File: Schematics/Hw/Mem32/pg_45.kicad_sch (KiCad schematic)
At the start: 10 parts, among them U4601 F04, U4602 F04, U4603 F04, U4604 F04, U4605 F04, U4606 F04, U4607 F04, U4608 F04, U4609 F04, U4610 F00

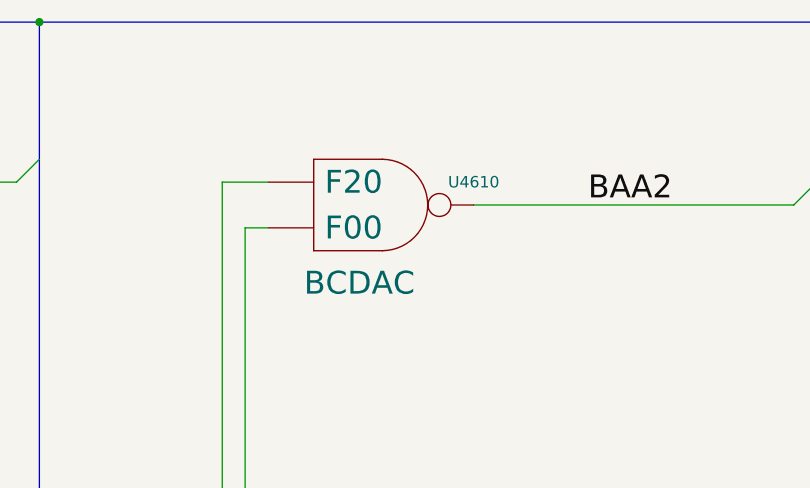
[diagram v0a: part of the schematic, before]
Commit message: Upgrade to KiCad9
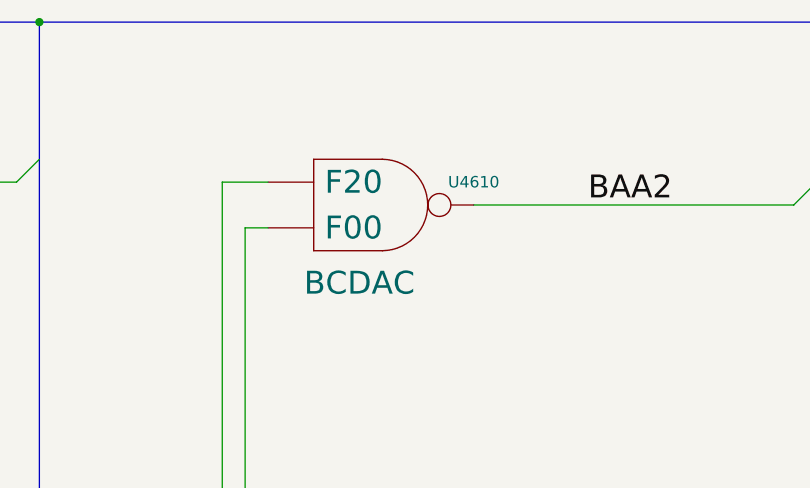
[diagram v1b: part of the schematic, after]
